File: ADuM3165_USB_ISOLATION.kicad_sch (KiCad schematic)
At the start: 70 parts, among them J1 USB_C_Receptacle_USB2.0, J2 USB_C_Receptacle_USB2.0, J3 USB_A, Q1 AS2302, SW1 Reset_Button, U1 MCP6004T-E/SL, U2 LTV-356T, U3 D5V0P4UR6SO-7, U4 ADuM3165, U5 D5V0P4UR6SO-7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

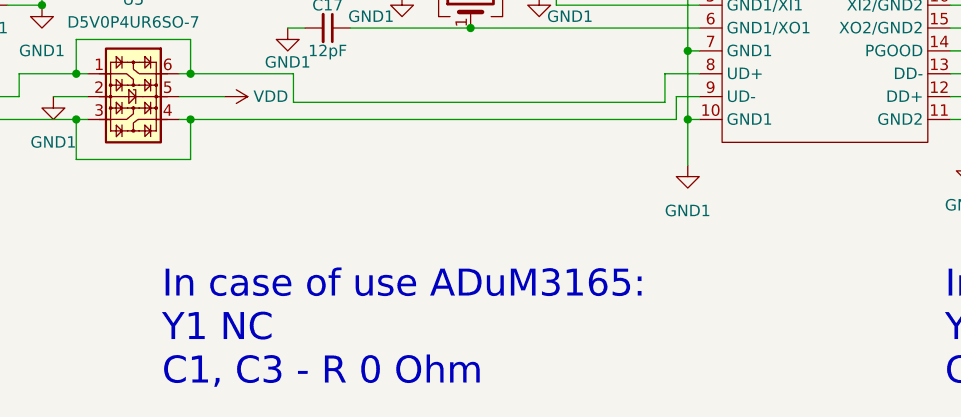
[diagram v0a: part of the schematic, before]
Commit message: change note on schematic
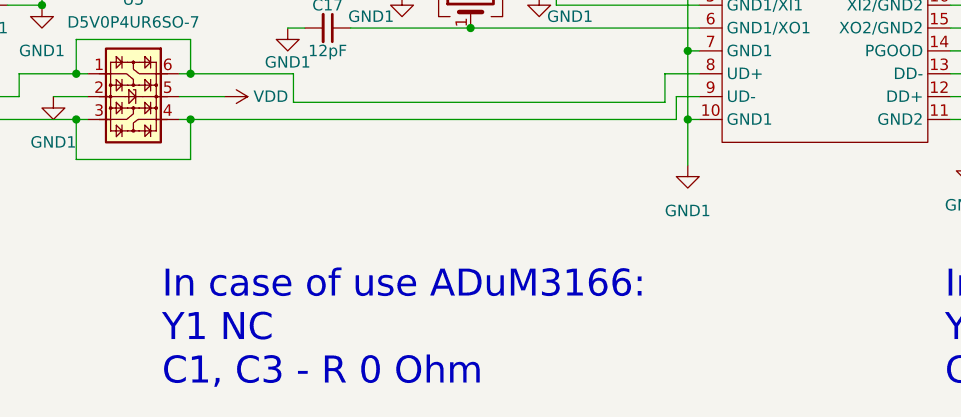
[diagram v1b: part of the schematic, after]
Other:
- note added: "In case of use ADuM3166: Y1 NC C1, C3 - R 0 Ohm"
- note removed: "In case of use ADuM3165: Y1 NC C1, C3 - R 0 Ohm"
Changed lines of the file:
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@@
     (effects (font (size 1.5 1.5)) (justify left bottom))
   )
-  (text "In case of use ADuM3165:\nY1 NC\nC1, C3 - R 0 Ohm" (at 107.315 245.745 0)
+  (text "In case of use ADuM3166:\nY1 NC\nC1, C3 - R 0 Ohm" (at 107.315 245.745 0)
     (effects (font (size 3 3)) (justify left bottom))
   )
